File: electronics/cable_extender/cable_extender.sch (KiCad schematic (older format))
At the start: 10 parts, among them J1 Conn_01x11, J2 Conn_01x06, J3 Conn_01x06, J4 Conn_01x11, J5 Conn_01x11, J6 Conn_01x11, J7 Conn_01x13, J8 Conn_01x13

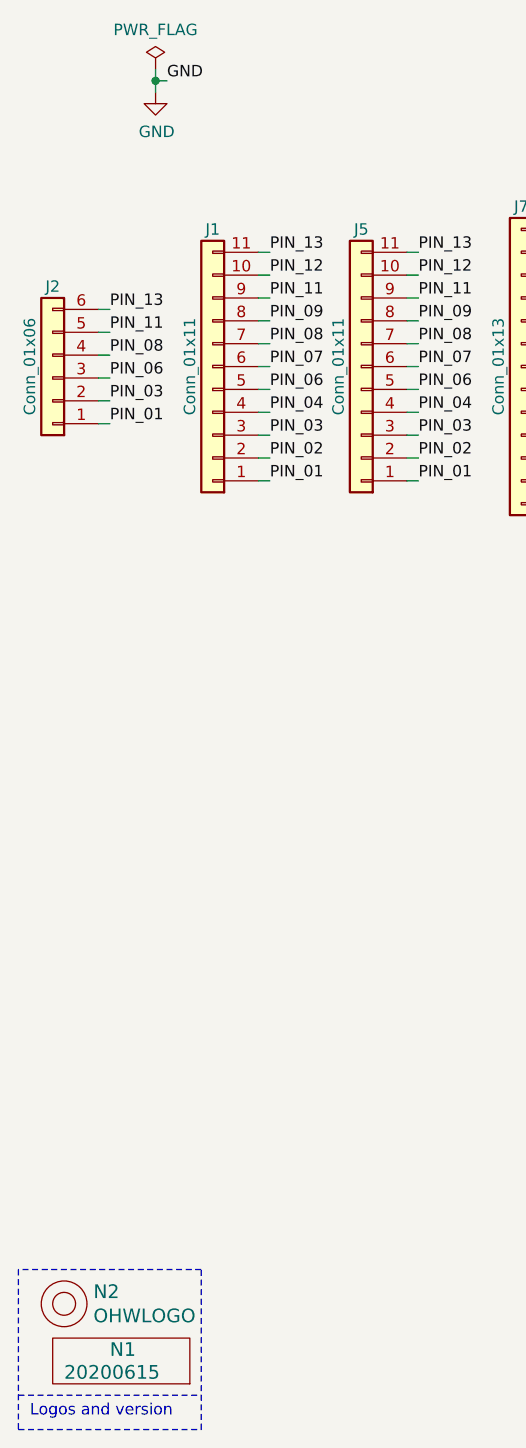
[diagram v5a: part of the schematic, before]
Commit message: removed versionnumber and OHW logo, not enough space, added test pad so a ground plane can be added
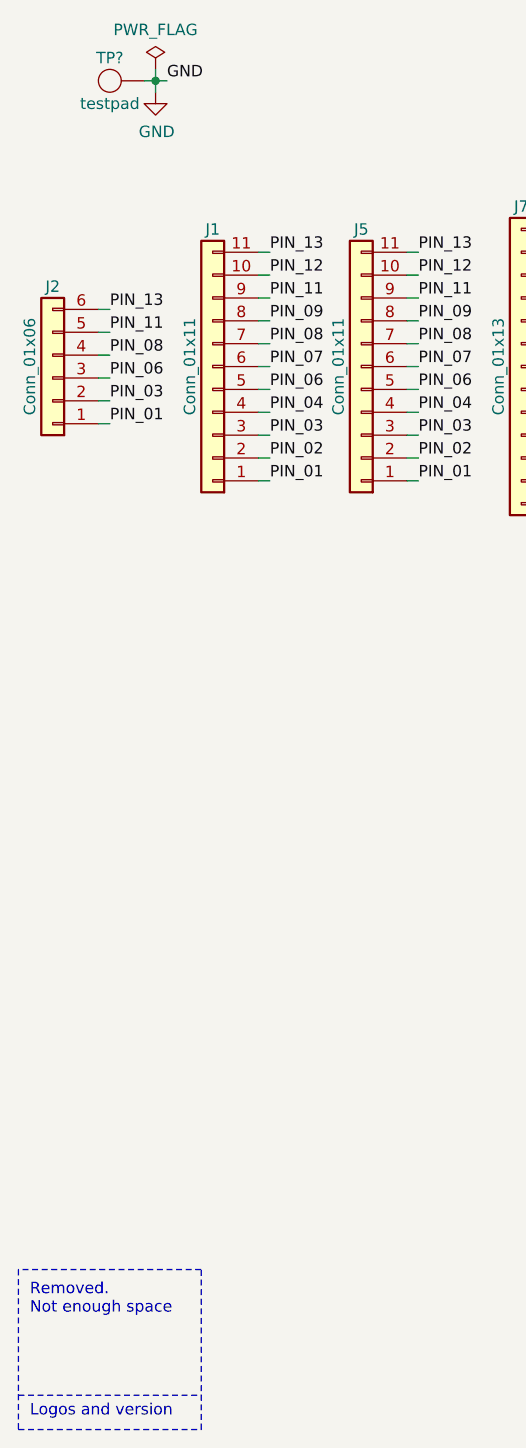
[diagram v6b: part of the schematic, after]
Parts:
- removed N1: 20200615, SquantorLabels:Label_Generic, symbol SquantorLabels:VYYYYMMDD
- removed N2: OHWLOGO, Symbol:OSHW-Symbol_6.7x6mm_SilkScreen, symbol SquantorLabels:OHWLOGO
- added TP?: testpad, TestPoint:TestPoint_Pad_D1.0mm, symbol SquantorProto:testpad
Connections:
- net GND: now also TP?.1
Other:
- note added: "Removed.\nNot enough space"
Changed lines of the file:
@@
 Comment4 ""
 $EndDescr
-$Comp
-L SquantorLabels:VYYYYMMDD N1
-U 1 1 5EE12BF3
-P 1050 7450
-F 0 "N1" H 1000 7550 60  0000 L CNN
-F 1 "20200615" H 800 7450 60  0000 L CNN
-F 2 "SquantorLabels:Label_Generic" H 1050 7450 60  0001 C CNN
-F 3 "" H 1050 7450 60  0001 C CNN
-	1    1050 7450
-	1    0    0    -1
-$EndComp
-$Comp
-L SquantorLabels:OHWLOGO N2
-U 1 1 5EE13678
-P 800 7150
-F 0 "N2" H 928 7203 60  0000 L CNN
-F 1 "OHWLOGO" H 928 7097 60  0000 L CNN
-F 2 "Symbol:OSHW-Symbol_6.7x6mm_SilkScreen" H 800 7150 60  0001 C CNN
-F 3 "" H 800 7150 60  0001 C CNN
-	1    800  7150
-	1    0    0    -1
-$EndComp
 Text Notes 650  7650 0    50   ~ 0
 Logos and version
@@
 Wire Wire Line
 	1000 3300 950  3300
+Text Notes 650  7200 0    50   ~ 0
+Removed.\nNot enough space
+$Comp
+L SquantorProto:testpad TP?
+U 1 1 5EE9DF4A
+P 1000 1800
+F 0 "TP?" H 1000 1700 50  0000 C CNN
+F 1 "testpad" H 1000 1900 50  0000 C CNN
+F 2 "TestPoint:TestPoint_Pad_D1.0mm" H 1000 1800 50  0001 C CNN
+F 3 "" H 1000 1800 50  0001 C CNN
+	1    1000 1800
+	-1   0    0    1
+$EndComp
+Wire Wire Line
+	1150 1800 1200 1800
 $EndSCHEMATC
